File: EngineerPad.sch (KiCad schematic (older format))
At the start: 69 parts, among them J1 AVR ISP 6, J2 USB_A, SW1 SW_Push, SW10 SW_Push, SW11 SW_Push, SW12 SW_Push, SW13 SW_Push, SW14 SW_Push, SW15 SW_Push, SW16 SW_Push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

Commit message: working version
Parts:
- D1, D10, D11, D12, D13, D14, D15, D16, D17, D18, D19, D2, D20, D21, D22, D23, D3, D4, D5, D6, D7, D8, D9: footprint Diode_THT:D_DO-35_SOD27_P7.62mm_Horizontal -> JSA:D_DO-35_SOD27_P7.62mm_Horizontal
- SW1, SW10, SW11, SW12, SW13, SW14, SW15, SW16, SW17, SW18, SW19, SW2, SW20, SW3, SW4, SW5, SW6, SW7, SW8, SW9: footprint Button_Switch_Keyboard:SW_Cherry_MX_1.00u_PCB -> JSA:SW_Cherry_MX_1.00u_PCB

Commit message: silkscreen and aref to ground
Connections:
- net GND: now also U1.21 (AREF)
- no-connect marks 10 -> 9
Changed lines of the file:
@@
 $EndDescr
-$Comp
-L MCU_Microchip_ATmega:ATmega328P-PU U1
-U 1 1 5F118C07
-P 1850 3700
-F 0 "U1" H 1206 3746 50  0000 R CNN
-F 1 "ATmega328P-PU" H 1206 3655 50  0000 R CNN
-F 2 "Package_DIP:DIP-28_W7.62mm_Socket" H 1850 3700 50  0001 C CIN
-F 3 "http://ww1.microchip.com/downloads/en/DeviceDoc/ATmega328_P%20AVR%20MCU%20with%20picoPower%20Technology%20Data%20Sheet%2040001984A.pdf" H 1850 3700 50  0001 C CNN
-	1    1850 3700
-	1    0    0    -1
-$EndComp
 $Comp
 L power:+5V #PWR01
@@
 Wire Wire Line
 	1950 2100 1950 2200
-Connection ~ 1950 2200
 $Comp
 L power:GND #PWR05
@@
 Col1
 NoConn ~ 2450 2500
-NoConn ~ 1250 2500
 Text GLabel 2450 4400 2    50   Input ~ 0
 D+
@@
 Wire Wire Line
 	2450 2600 3850 2600
+Connection ~ 1950 2200
+$Comp
+L MCU_Microchip_ATmega:ATmega328P-PU U1
+U 1 1 5F118C07
+P 1850 3700
+F 0 "U1" H 1206 3746 50  0000 R CNN
+F 1 "ATmega328P-PU" H 1206 3655 50  0000 R CNN
+F 2 "Package_DIP:DIP-28_W7.62mm_Socket" H 1850 3700 50  0001 C CIN
+F 3 "http://ww1.microchip.com/downloads/en/DeviceDoc/ATmega328_P%20AVR%20MCU%20with%20picoPower%20Technology%20Data%20Sheet%2040001984A.pdf" H 1850 3700 50  0001 C CNN
+	1    1850 3700
+	1    0    0    -1
+$EndComp
+$Comp
+L power:GND #PWR0103
+U 1 1 5F56287C
+P 1100 2500
+F 0 "#PWR0103" H 1100 2250 50  0001 C CNN
+F 1 "GND" H 1105 2327 50  0000 C CNN
+F 2 "" H 1100 2500 50  0001 C CNN
+F 3 "" H 1100 2500 50  0001 C CNN
+	1    1100 2500
+	1    0    0    -1
+$EndComp
+Wire Wire Line
+	1100 2500 1250 2500
 $EndSCHEMATC

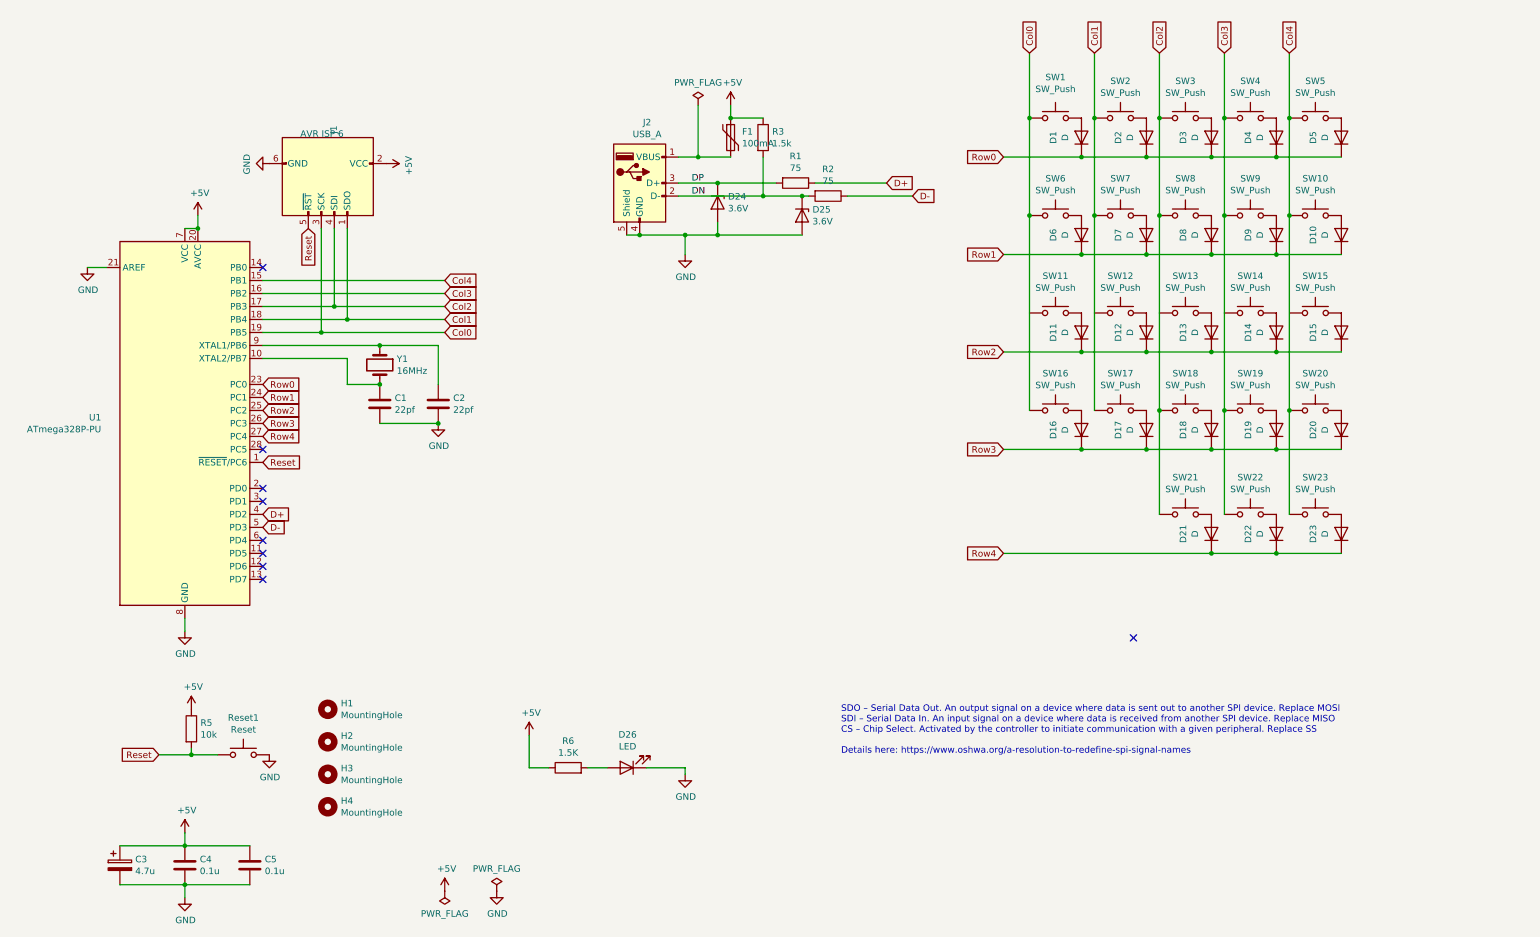
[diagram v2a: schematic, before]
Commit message: remove aref add a logo
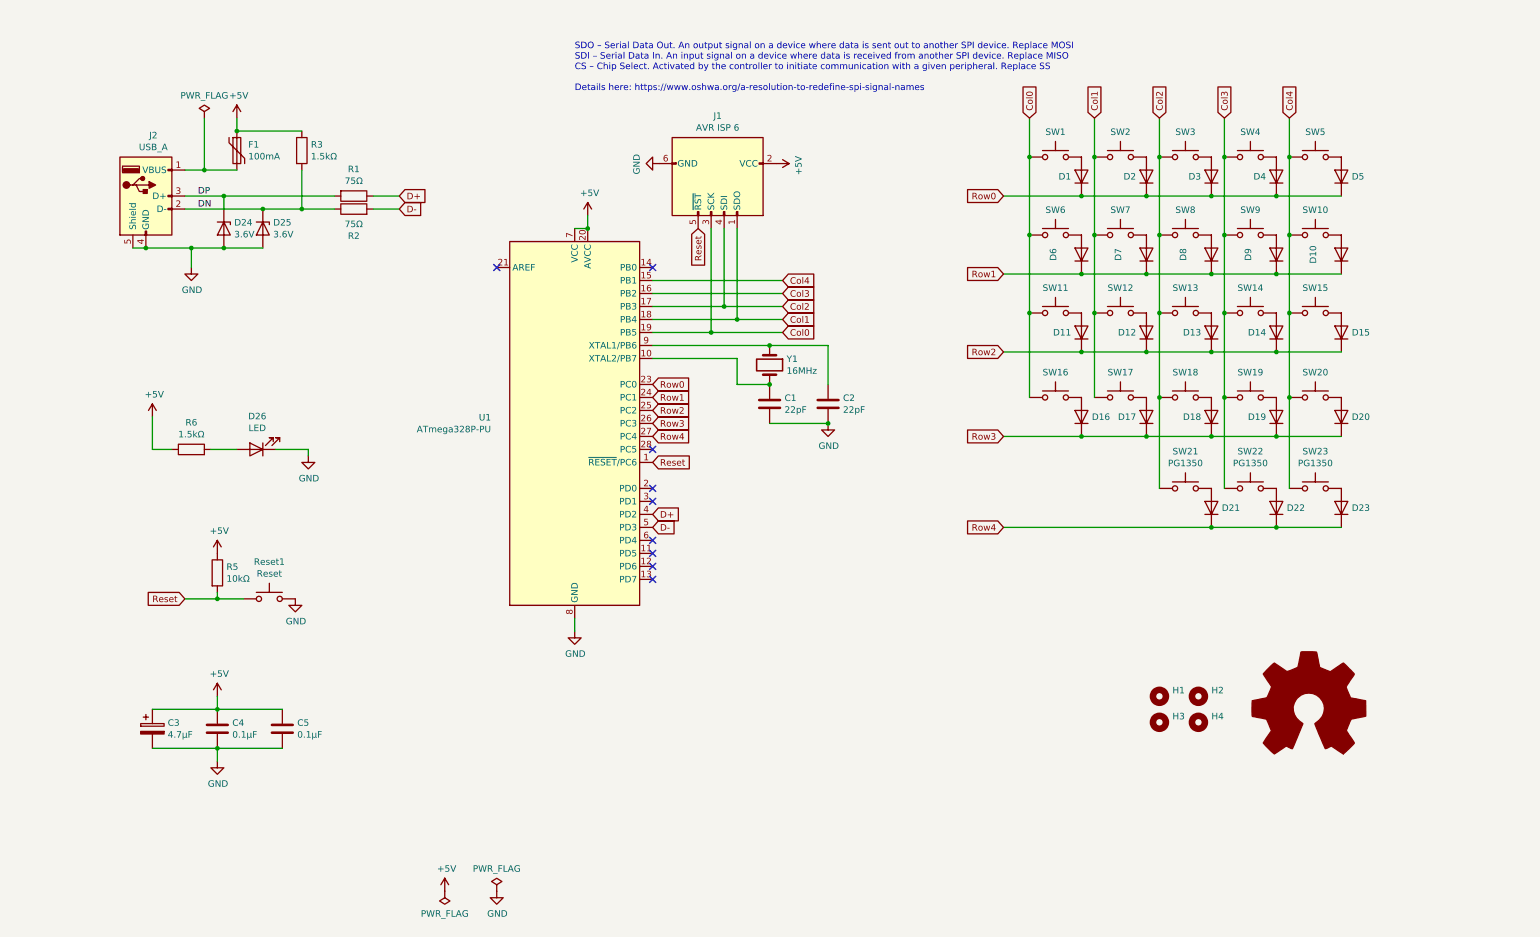
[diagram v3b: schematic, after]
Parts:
- C1, C2: value 22pf -> 22pF
- C3: value 4.7u -> 4.7μF
- C4, C5: value 0.1u -> 0.1μF
- D1, D10, D11, D12, D13, D14, D15, D16, D17, D18, D19, D2, D20, D21, D22, D23, D3, D4, D5, D6, D7, D8, D9: footprint JSA:D_DO-35_SOD27_P7.62mm_Horizontal -> JSA:Diode_THT
- R1, R2: value 75 -> 75Ω
- R3: value 1.5k -> 1.5kΩ
- R5: value 10k -> 10kΩ
- R6: value 1.5K -> 1.5kΩ
- SW21, SW22, SW23: value SW_Push -> PG1350
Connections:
- net D-: now also R2.2; no longer R2.1
- net DN: now also R2.1; no longer R2.2
- net GND: no longer U1.21 (AREF)
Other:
- moved on the sheet: C1, C2, C3, C4, C5, D1, D10, D16, D17, D18, D19, D2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
